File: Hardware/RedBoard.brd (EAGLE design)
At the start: 68.6 x 58.4 mm, 169 parts, among them IC3 LM1117, J2 ISP, J3 5.5x2.1mm Barrel, J4 QWIIC_RIGHT_ANGLE, J5 USB Female Type C Connector, Q1 20V/4.2A/52mΩ/1.4W, Q2 310mA/60V/1.6Ω, Q3 310mA/60V/1.6Ω, U3 3.3V, U4 ATMEGA328P_TQFP, U5 CH340C, Y1 16MHz

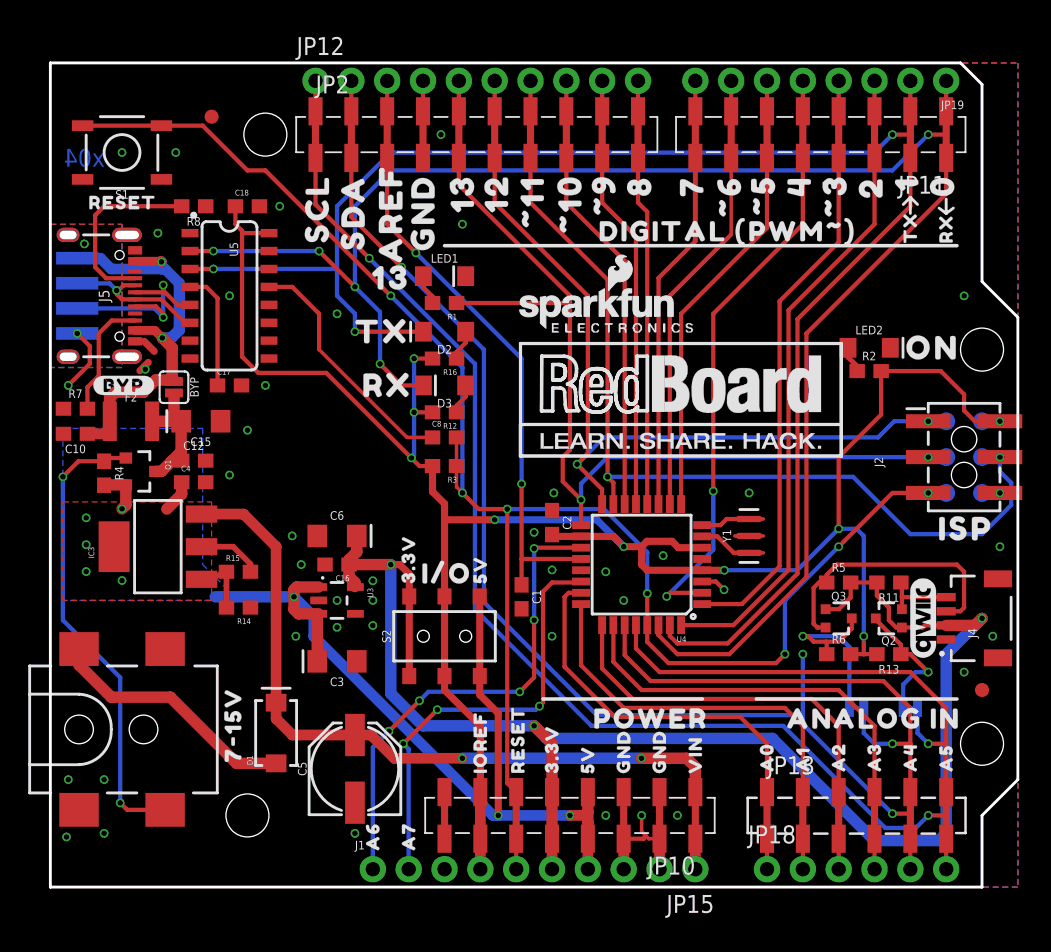
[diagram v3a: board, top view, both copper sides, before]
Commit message: Ran schematic and board auto-checklists
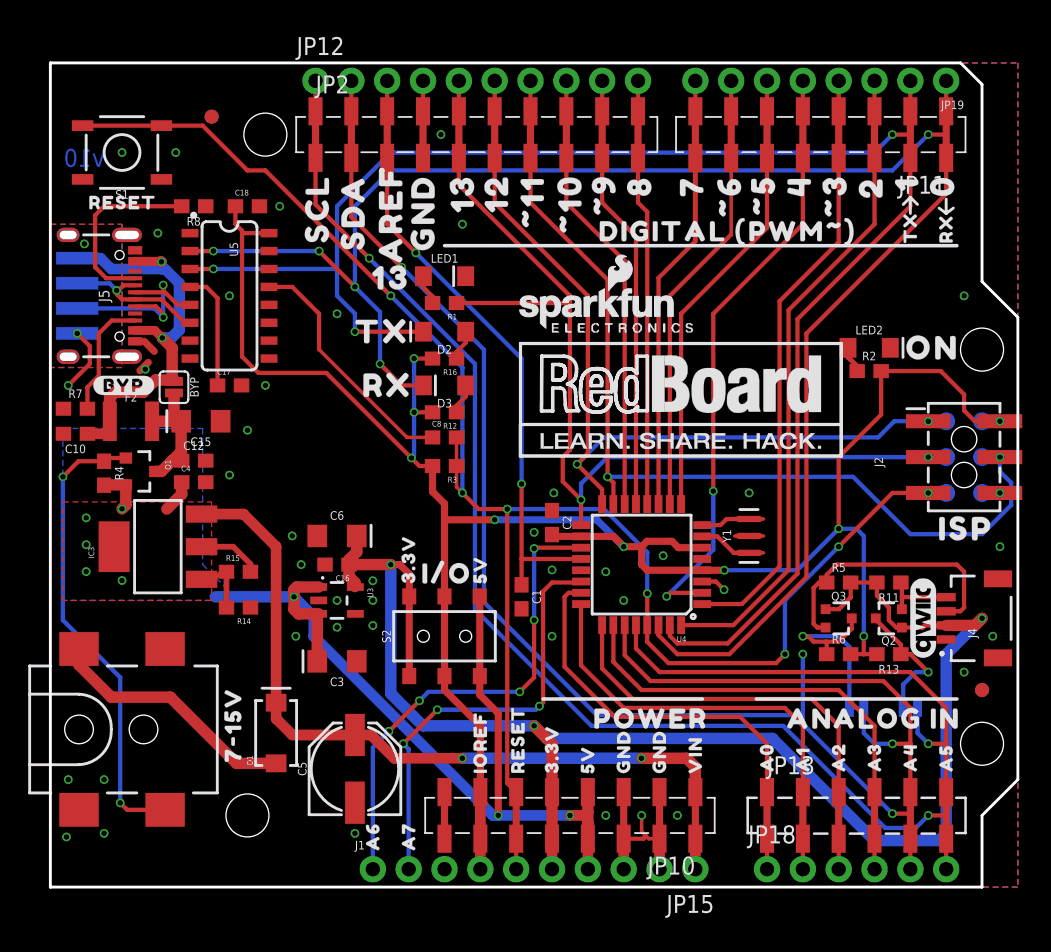
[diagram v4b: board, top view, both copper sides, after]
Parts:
- added FD1, FD2: FIDUCIAL1X2, SparkFun-Aesthetics:FIDUCIAL-1X2
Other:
- board text added: "Jim Lindblom N. Seidle"
- board text added: "v10"
- board text removed: "x04"
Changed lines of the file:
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@@
 <?xml version="1.0" encoding="utf-8"?>
 <!DOCTYPE eagle SYSTEM "eagle.dtd">
-<eagle version="9.6.2">
+<eagle version="9.5.2">
 <drawing>
 <settings>
-<setting alwaysvectorfont="yes"/>
+<setting alwaysvectorfont="no"/>
 <setting keepoldvectorfont="yes"/>
 <setting verticaltext="up"/>
@@
 <wire x1="66.04" y1="56.896" x2="66.04" y2="42.926" width="0.2032" layer="20"/>
 <text x="0" y="-0.0635" size="0.0254" layer="214" font="vector">D:/SmartProjects/Snc/a4_bn_logo2.bmp</text>
-<text x="2.413" y="51.689" size="1.27" layer="16" font="vector" ratio="20" rot="MR0" align="center">x04</text>
+<text x="2.413" y="51.689" size="1.27" layer="16" font="vector" ratio="20" rot="MR0" align="center">v10</text>
 <rectangle x1="0.635" y1="22.352" x2="2.032" y2="30.607" layer="43"/>
 <rectangle x1="5.715" y1="23.114" x2="7.366" y2="30.607" layer="43"/>
@@
 <wire x1="34.925" y1="13.335" x2="46.228" y2="13.335" width="0.254" layer="21"/>
 <wire x1="50.038" y1="13.335" x2="64.262" y2="13.335" width="0.254" layer="21"/>
+<text x="26.67" y="-39.37" size="1.778" layer="51" font="vector" ratio="15">Jim Lindblom
+N. Seidle</text>
 </plain>
 <attributes>
@@
 <element name="U$78" library="redboard_logo" package="REDBOARD_LOGO" value="REDBOARD_LOGO" x="33.274" y="30.353" smashed="yes"/>
 <element name="U$1" library="redboard_logo" package="REDBOARD_LOGO" value="REDBOARD_LOGO" x="62.992" y="42.672" smashed="yes" rot="MR0"/>
+<element name="FD1" library="SparkFun-Aesthetics" package="FIDUCIAL-1X2" value="FIDUCIAL1X2" x="11.43" y="54.61" smashed="yes" rot="MR0"/>
+<element name="FD2" library="SparkFun-Aesthetics" package="FIDUCIAL-1X2" value="FIDUCIAL1X2" x="66.04" y="13.97" smashed="yes" rot="MR0"/>
 </elements>
 <signals>
@@
 </drawing>
 <compatibility>
+<note version="6.3" minversion="6.2.2" severity="warning">
+Since Version 6.2.2 text objects can contain more than one line,
+which will not be processed correctly with this version.
+</note>
 <note version="8.3" severity="warning">
 Since Version 8.3, EAGLE supports URNs for individual library
